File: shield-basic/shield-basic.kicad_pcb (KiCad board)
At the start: 2 copper layers, 52 x 60 mm, 52 parts, among them CON1 SD_Card, IC1 DRV8833, P1 CONN_01X04, P10 CONN_01X02, P2 CONN_01X04, P3 CONN_01X04, P4 CONN_01X04, P5 CONN_01X04, P6 CONN_01X02, P7 CONN_01X02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

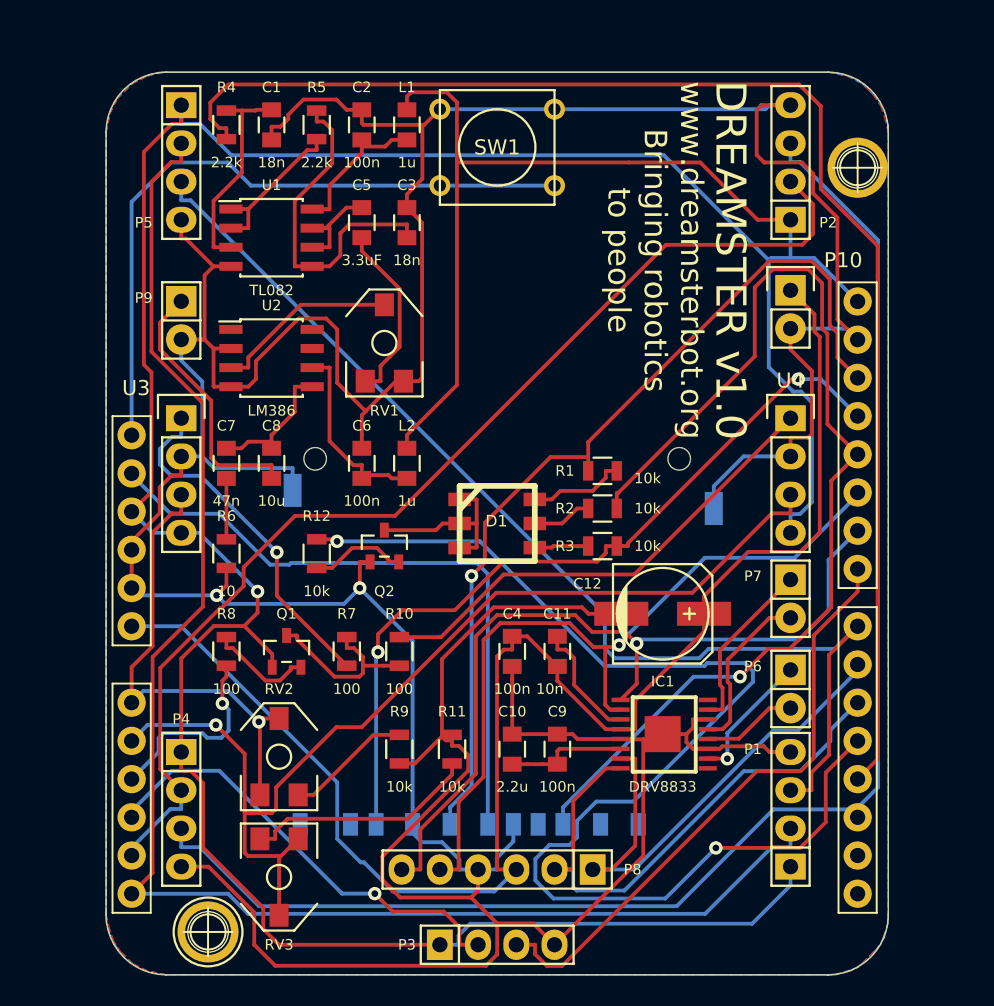
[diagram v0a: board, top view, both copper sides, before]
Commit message: Fix #7: The connector was move to the board edge. Fix #8: Added a hole for the wires. Fix #11: The board now is bigger to get the at the proper distance. Fix: #12: Now the LED won't be covered by the board.
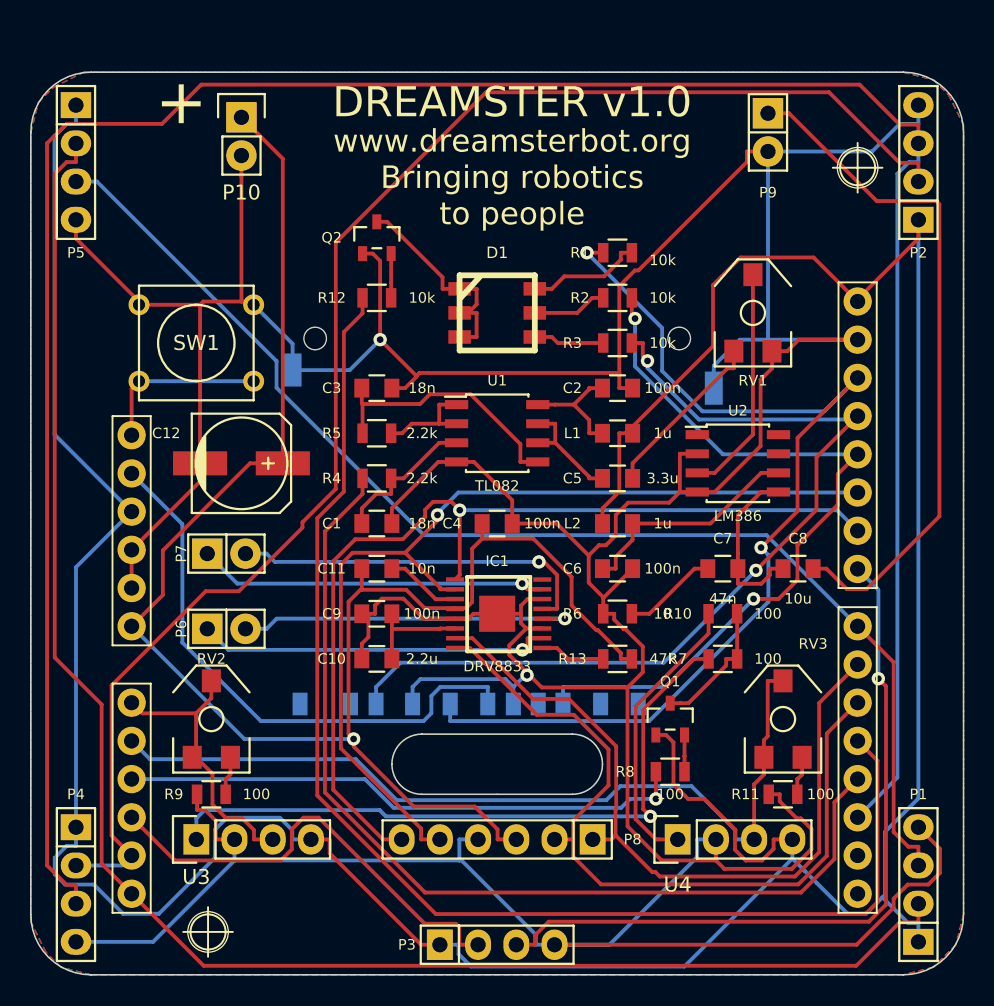
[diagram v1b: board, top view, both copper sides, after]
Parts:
- removed 1pin (x2): VAL**, Connect:1pin
- added R13: 47k, Resistors_SMD:R_0805, F.Cu at (182.0, 81.0)
- C5: value 3.3uF -> 3.3u
- R11, R9: value 10k -> 100
- RV2, RV3: value POT -> 10k
- moved P9 41.0 mm to (192.0, 46.0)
- moved P10 38.3 mm to (157.0, 45.0)
- moved P6 37.7 mm to (156.0, 79.0), turned to 180 degrees
- moved P7 37.6 mm to (156.0, 74.0), turned to 180 degrees
- moved C8 35.7 mm to (194.0, 75.0), turned to 0 degrees
- moved RV3 35.1 mm to (193.0, 85.0), turned to 0 degrees
- moved C7 33.7 mm to (189.0, 75.0), turned to 180 degrees
- moved U2 31.8 mm to (190.0, 68.0)
- moved R8 30.6 mm to (185.5, 88.5), turned to 180 degrees
- moved C12 29.7 mm to (157.0, 68.0)
- moved U4 29.0 mm to (186.0, 93.0), turned to 0 degrees
- moved U3 28.0 mm to (154.0, 93.0), turned to 0 degrees
- moved C1 27.4 mm to (166.0, 72.0), turned to 0 degrees
- moved R6 26.3 mm to (182.0, 78.0), turned to 180 degrees
- moved Q1 25.9 mm to (185.5, 85.0)
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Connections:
- C11 pad 1: +BATT -> Net-(C11-Pad1)
- C11 pad 2: Net-(C11-Pad2) -> +BATT
- IC1 pad 1: (no net) -> Net-(IC1-Pad1)
- IC1 pad 11: Net-(C11-Pad2) -> Net-(C11-Pad1)
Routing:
- net /ECHO_B: track 98.7 -> 160.4 mm
- net /RESET: track 45.3 -> 11.4 mm
- net GND: track 338.8 -> 368.6 mm
- net Net-(C8-Pad2): track 17.5 -> 45.6 mm
- net /sound/In: track 91.7 -> 65.4 mm
- net /irsensor/~EMITTER: track 13.2 -> 37.7 mm
- net /TRG_B: track 75.0 -> 98.8 mm
- net Net-(R7-Pad2): track 23.7 -> 45.0 mm
- net /GREEN: track 71.6 -> 51.5 mm, vias 1 -> 2
- net /hbridge/RM-: track 6.35 -> 23.0 mm, vias 0 -> 1
- net /hbridge/RMI2: track 33.8 -> 50.1 mm
- net /hbridge/RMI1: track 36.9 -> 51.8 mm
- net /hbridge/RM+: track 8.95 -> 23.4 mm
- net /hbridge/LM-: track 11.2 -> 24.5 mm, vias 0 -> 1
- net Net-(R10-Pad2): track 32.0 -> 19.0 mm
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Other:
- board size 52 x 60 mm -> 62 x 60 mm
- board text added: "+"

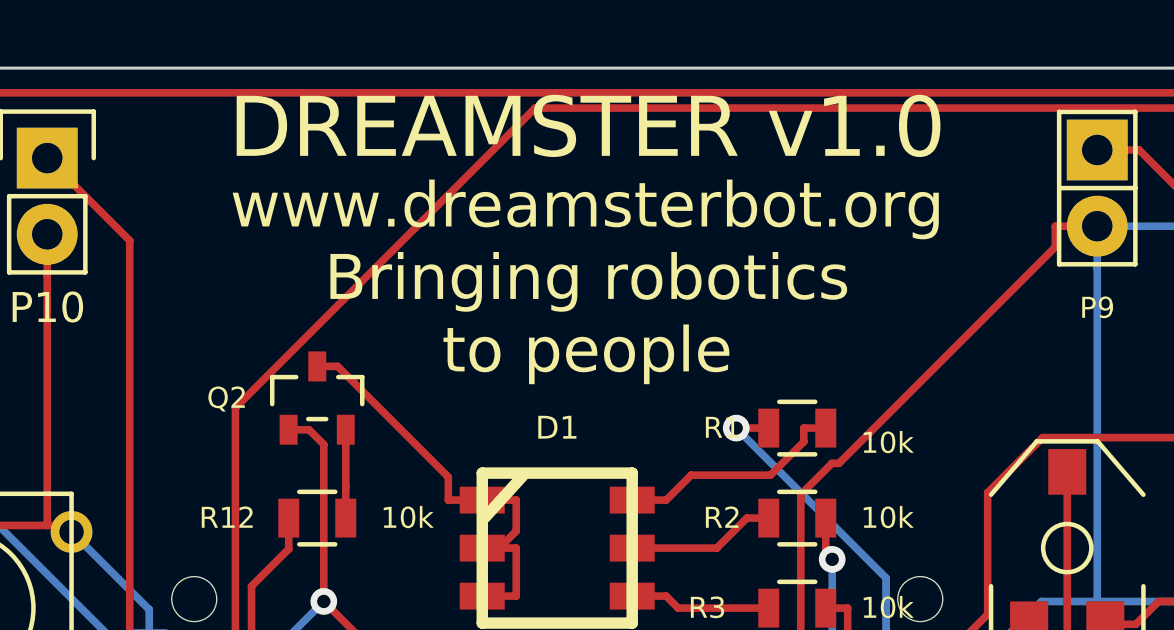
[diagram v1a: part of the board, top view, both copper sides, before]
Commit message: Change the slogan in the board.
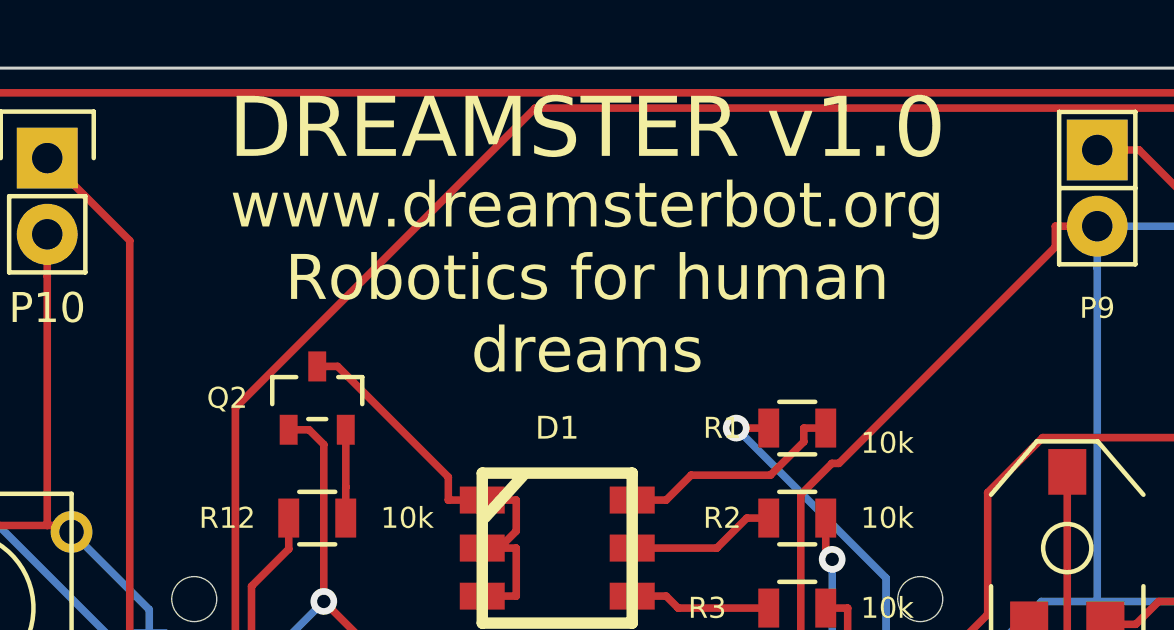
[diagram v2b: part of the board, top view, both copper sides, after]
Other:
- board text added: "www.dreamsterbot.org Robotics for human dreams"
- board text removed: "www.dreamsterbot.org Bringing robotics to people"

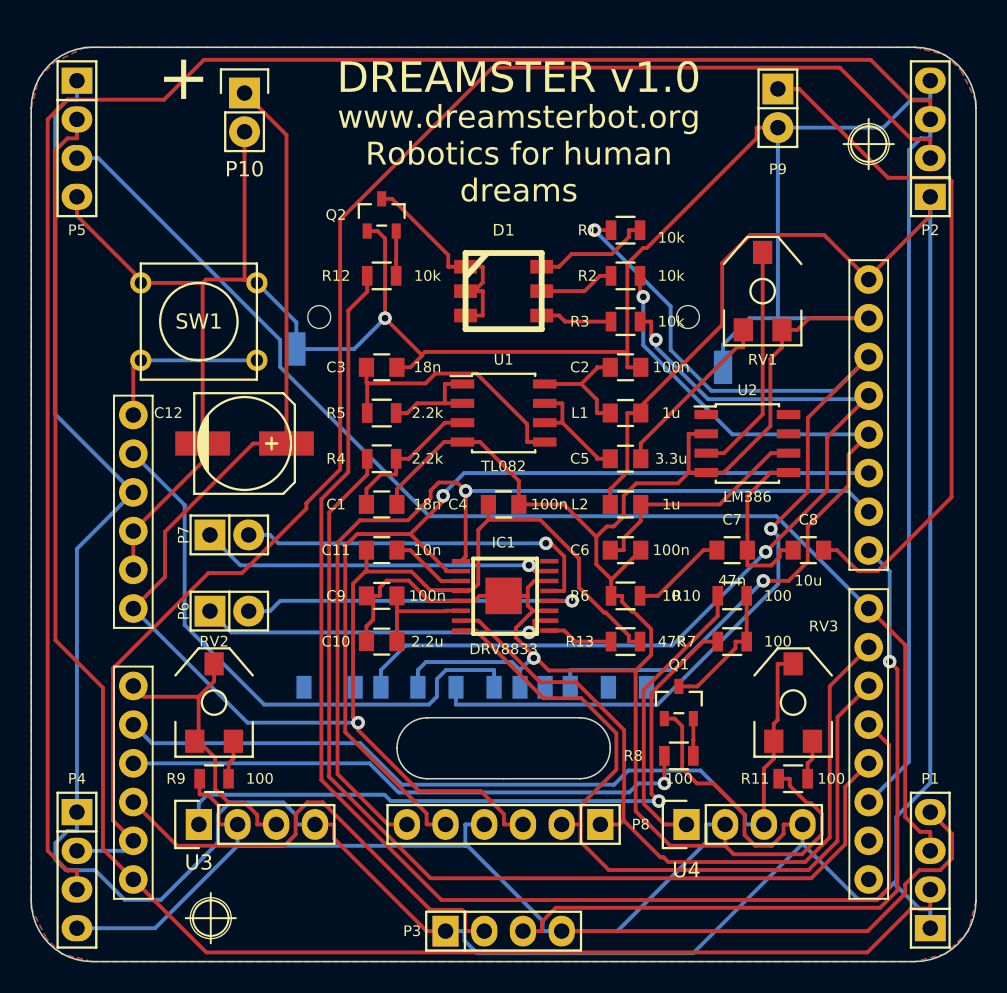
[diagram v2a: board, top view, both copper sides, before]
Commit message: Fix #13: The capacitor was moved next to the IC Fix #14: I added both simbols Fix #15: I add power pad. Fix #16
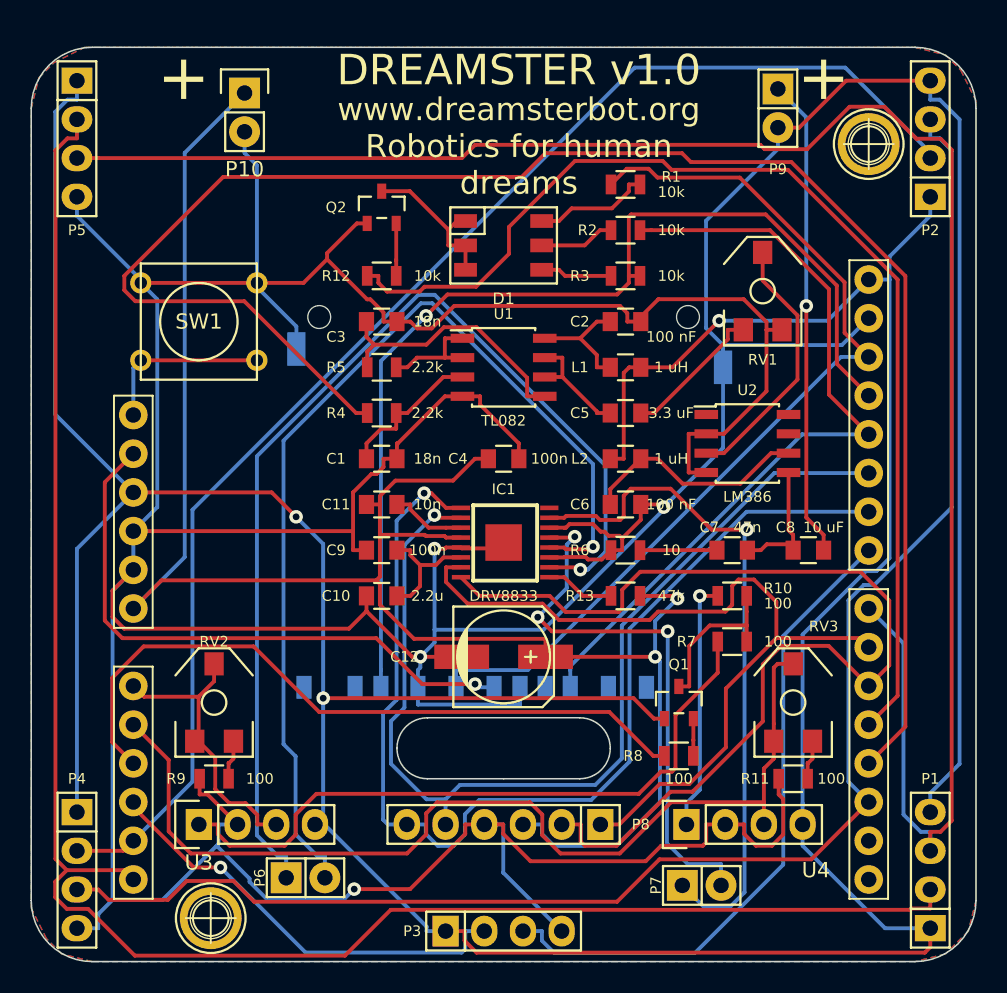
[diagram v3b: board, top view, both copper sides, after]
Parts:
- added P11: CONN_01X01, Connect:1pin, F.Cu at (154.8, 99.2)
- added P12: CONN_01X01, Connect:1pin, F.Cu at (198.0, 48.4)
- C2, C6: value 100n -> 100 nF
- C5: value 3.3u -> 3.3 uF
- C8: value 10u -> 10 uF
- L1, L2: value 1u -> 1 uH
- moved P7 38.6 mm to (187.0, 97.0)
- moved C12 22.0 mm to (174.0, 82.0)
- moved P6 18.2 mm to (161.0, 96.5)
- moved IC1 3.50 mm to (174.0, 74.5)
- moved C1 3.00 mm to (166.0, 69.0)
- moved C10 3.00 mm to (166.0, 78.0)
- moved C11 3.00 mm to (166.0, 72.0)
- moved C2 3.00 mm to (182.0, 60.0)
- moved C3 3.00 mm to (166.0, 60.0)
- moved C4 3.00 mm to (174.0, 69.0)
- moved C5 3.00 mm to (182.0, 66.0)
- moved C6 3.00 mm to (182.0, 72.0)
- moved C9 3.00 mm to (166.0, 75.0)
- moved D1 3.00 mm to (174.0, 55.0)
- moved L1 3.00 mm to (182.0, 63.0)
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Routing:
- net GND: track 368.6 -> 432.8 mm, vias 2 -> 4
- net /ECHO_B: track 160.4 -> 105.5 mm
- net /hbridge/RM+: track 23.4 -> 70.6 mm
- net /sound/In: track 65.4 -> 111.1 mm
- net /hbridge/RM-: track 23.0 -> 66.9 mm
- net /ECHO_C: track 83.2 -> 125.1 mm
- net /hbridge/LM+: track 23.3 -> 44.8 mm
- net /hbridge/RMI1: track 51.8 -> 67.9 mm
- net Net-(C8-Pad2): track 45.6 -> 31.5 mm, vias 0 -> 1
- net /LED_enable: track 86.4 -> 73.3 mm
- net /hbridge/LM-: track 24.5 -> 36.3 mm, vias 1 -> 3
- net +BATT: track 112.6 -> 123.2 mm, vias 1 -> 2
- net /hbridge/LMI1: track 63.4 -> 73.3 mm
- net /TRG_C: track 109.7 -> 118.8 mm
- net /irsensor/~EMITTER: track 37.7 -> 46.3 mm, vias 1 -> 0
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
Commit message: Fixed some minor issues
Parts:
- P10: footprint Socket_Strips:Socket_Strip_Straight_1x02 -> Connect:PINHEAD1-2
- P9: value speaker -> Speaker; footprint Socket_Strips:Socket_Strip_Straight_1x02 -> Connect:PINHEAD1-2
- moved P10 2.38 mm to (155.0, 46.4), turned to 0 degrees
- moved P9 1.28 mm to (191.6, 47.2), turned to 0 degrees
- moved P7 0.12 mm to (187.0, 96.9), turned to 0 degrees
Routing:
- net GND: track 432.8 -> 288.5 mm, vias 4 -> 8
- net +5VD: track 237.2 -> 189.1 mm, vias 3 -> 4
- net /hbridge/RMI1: track 67.9 -> 80.0 mm, vias 0 -> 2
- net /hbridge/RM-: track 66.9 -> 57.2 mm
- net +BATT: track 123.2 -> 132.6 mm
- net /hbridge/RM+: track 70.6 -> 63.7 mm
- net /irsensor/LSENS: track 19.3 -> 24.8 mm, vias 0 -> 1
- net Net-(C8-Pad2): track 31.5 -> 36.8 mm
- net /hbridge/LM-: track 36.3 -> 32.6 mm
- net /BLUE: track 61.1 -> 64.9 mm
- net /irsensor/RSENS: track 65.3 -> 68.8 mm
- net /LED_enable: track 73.3 -> 76.6 mm
- net /RED: track 68.6 -> 71.4 mm, vias 1 -> 3
- net /hbridge/RMI2: track 54.7 -> 57.3 mm
- net /sound/In: track 111.1 -> 113.4 mm
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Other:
- net class Default: via_drill 0.635 -> 0.508
- board text added: "-"
- board text added: "BATT"

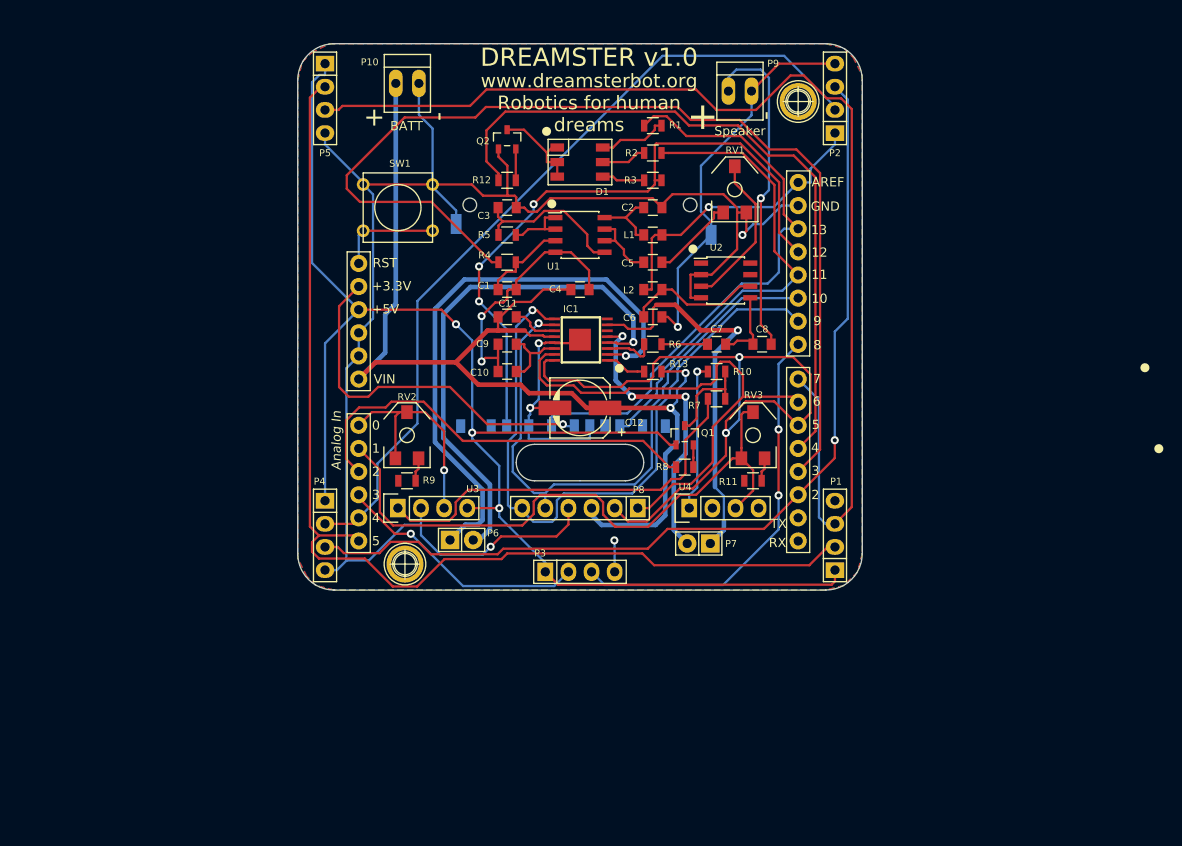
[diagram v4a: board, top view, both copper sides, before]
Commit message: fixed some marks and cetered pcb
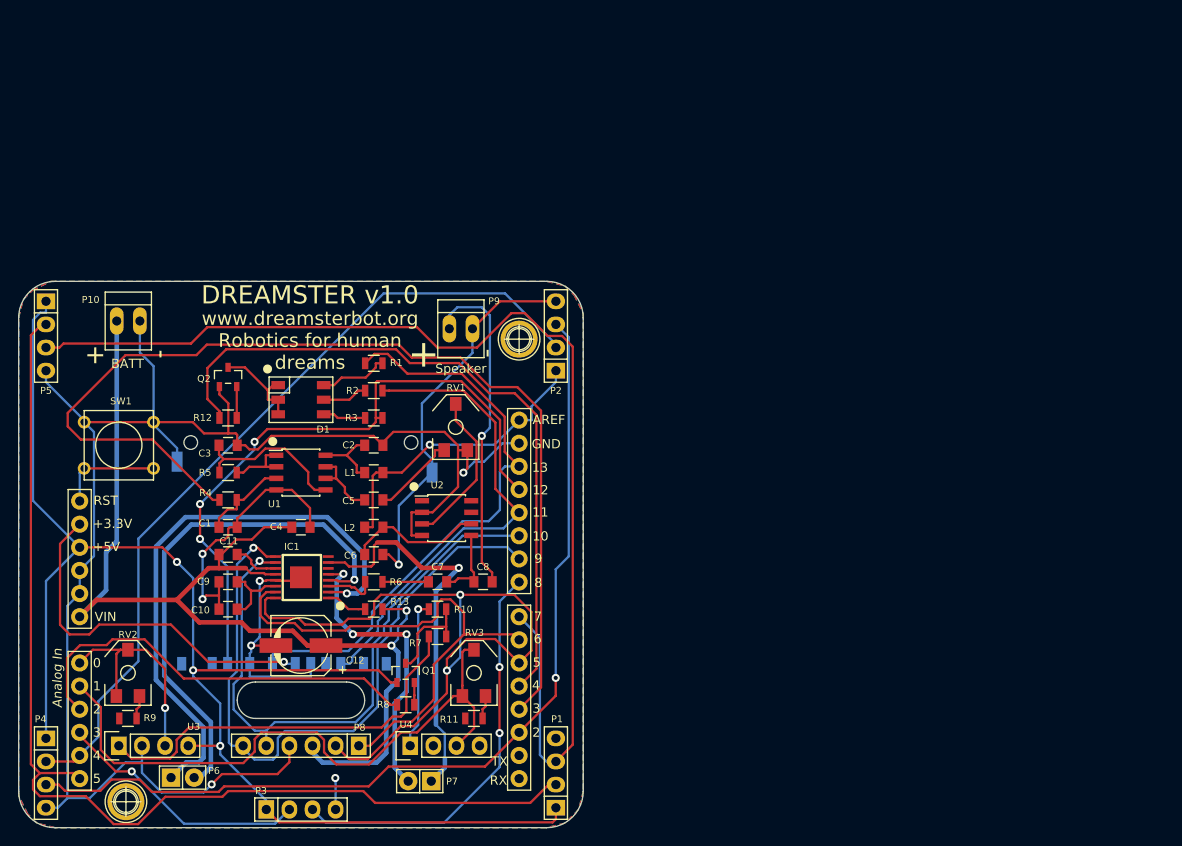
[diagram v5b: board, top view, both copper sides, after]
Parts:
- moved C1 40.3 mm to (135.4, 95.1)
- moved C10 40.3 mm to (135.4, 104.1)
- moved C11 40.3 mm to (135.4, 98.1)
- moved C12 40.3 mm to (143.4, 108.1)
- moved C2 40.3 mm to (151.4, 86.1)
- moved C3 40.3 mm to (135.4, 86.1)
- moved C4 40.3 mm to (143.4, 95.1)
- moved C5 40.3 mm to (151.4, 92.1)
- moved C6 40.3 mm to (151.4, 98.1)
- moved C7 40.3 mm to (158.4, 101.1)
- moved C8 40.3 mm to (163.4, 101.1)
- moved C9 40.3 mm to (135.4, 101.1)
- moved CON1 40.3 mm to (143.4, 110.1)
- moved D1 40.3 mm to (143.4, 81.1)
- moved IC1 40.3 mm to (143.4, 100.6)
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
